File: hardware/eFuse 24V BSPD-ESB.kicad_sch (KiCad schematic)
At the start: 9 parts, among them IC3 NCS20061MUTAG_IMG, IC6 NIS4461MT1TXG

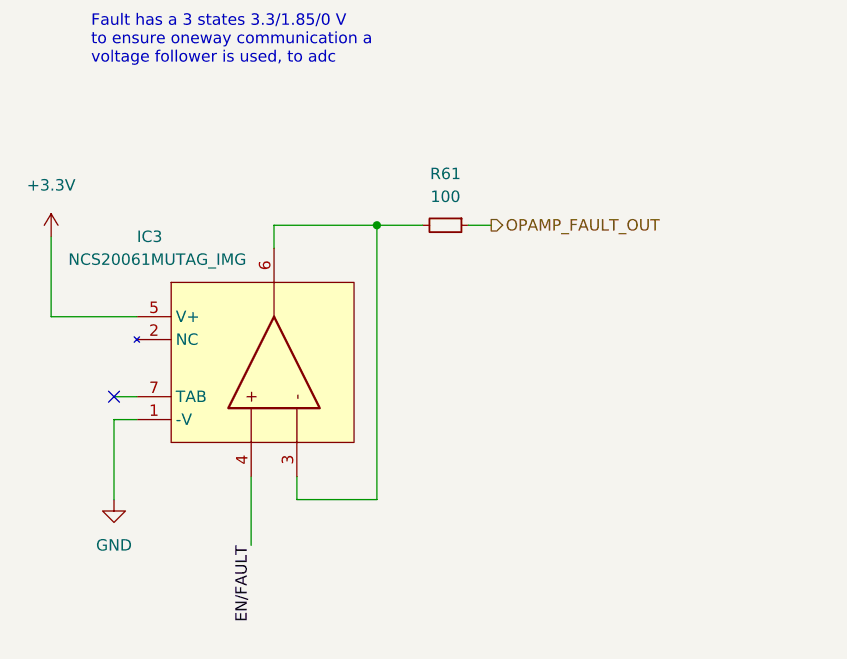
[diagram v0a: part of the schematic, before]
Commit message: debuged the board, changed one opto for mosfet, changed the way water and potentiometers were supplied. Also standrised opamps (yoinked opamps from data Data_Acquisition_Cards)
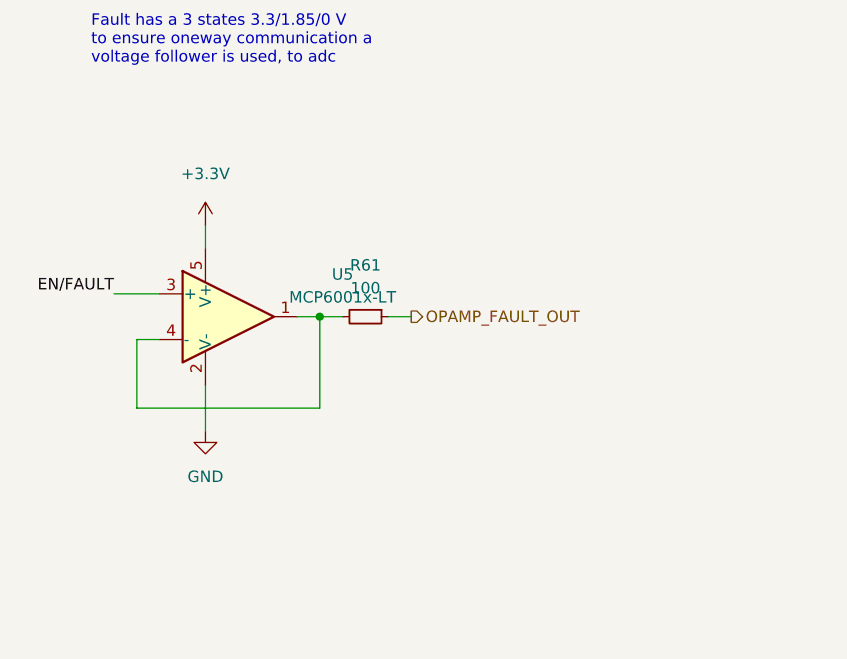
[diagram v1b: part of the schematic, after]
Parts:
- removed IC3: NCS20061MUTAG_IMG, NCS20061MUTAG:SON50P160X160X55-7N, symbol NCS20061MUTAG:NCS20061MUTAG_IMG
- added U5: MCP6001x-LT, Package_TO_SOT_SMD:SOT-353_SC-70-5, symbol Amplifier_Operational:MCP6001x-LT
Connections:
- net +3V3: now also U5.5 (V+)
- net EN/FAULT: now also U5.3 (+)
- net GND: now also U5.2 (V-)
- net at R61.2: now also U5.1, U5.4 (-)
- no-connect marks 1 -> 0
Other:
- moved on the sheet: R61
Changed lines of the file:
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@@
   (junction (at 220.98 99.06) (diameter 0) (color 0 0 0 0)
   )
-  (junction (at 92.71 67.31) (diameter 0) (color 0 0 0 0)
+  (junction (at 86.36 77.47) (diameter 0) (color 0 0 0 0)
   )
   (junction (at 234.315 73.025) (diameter 0) (color 0 0 0 0)
@@
   (junction (at 180.34 83.185) (diameter 0) (color 0 0 0 0)
   )
-  (no_connect (at 63.5 86.36))
-  (wire (pts (xy 92.71 67.31) (xy 97.79 67.31))
+  (wire (pts (xy 83.82 77.47) (xy 86.36 77.47))
     (stroke (width 0) (type default) (color 0 0 0 0))
   )
@@
     (stroke (width 0) (type default) (color 0 0 0 0))
   )
-  (wire (pts (xy 56.515 77.47) (xy 66.04 77.47))
-    (stroke (width 0) (type default) (color 0 0 0 0))
-  )
-  (wire (pts (xy 102.87 67.31) (xy 105.41 67.31))
+  (wire (pts (xy 93.98 77.47) (xy 96.52 77.47))
     (stroke (width 0) (type default) (color 0 0 0 0))
   )
@@
     (stroke (width 0) (type default) (color 0 0 0 0))
   )
+  (wire (pts (xy 86.36 77.47) (xy 86.36 87.63))
+    (stroke (width 0) (type default) (color 0 0 0 0))
+  )
   (wire (pts (xy 228.6 95.25) (xy 234.315 95.25))
     (stroke (width 0) (type default) (color 0 0 0 0))
   )
+  (wire (pts (xy 66.04 87.63) (xy 66.04 80.01))
+    (stroke (width 0) (type default) (color 0 0 0 0))
+  )
   (wire (pts (xy 180.34 62.865) (xy 180.34 83.185))
     (stroke (width 0) (type default) (color 0 0 0 0))
   )
-  (wire (pts (xy 56.515 68.58) (xy 56.515 77.47))
+  (wire (pts (xy 73.66 67.31) (xy 73.66 69.85))
     (stroke (width 0) (type default) (color 0 0 0 0))
   )
@@
     (stroke (width 0) (type default) (color 0 0 0 0))
   )
-  (wire (pts (xy 78.74 95.25) (xy 78.74 102.87))
-    (stroke (width 0) (type default) (color 0 0 0 0))
-  )
-  (wire (pts (xy 81.28 67.31) (xy 81.28 69.85))
+  (wire (pts (xy 68.58 74.93) (xy 63.5 74.93))
     (stroke (width 0) (type default) (color 0 0 0 0))
   )
@@
     (stroke (width 0) (type default) (color 0 0 0 0))
   )
-  (wire (pts (xy 63.5 86.36) (xy 66.04 86.36))
-    (stroke (width 0) (type default) (color 0 0 0 0))
-  )
   (wire (pts (xy 186.69 65.405) (xy 186.69 75.565))
     (stroke (width 0) (type default) (color 0 0 0 0))
@@
     (stroke (width 0) (type default) (color 0 0 0 0))
   )
+  (wire (pts (xy 86.36 87.63) (xy 66.04 87.63))
+    (stroke (width 0) (type default) (color 0 0 0 0))
+  )
   (wire (pts (xy 193.675 70.485) (xy 196.215 70.485))
     (stroke (width 0) (type default) (color 0 0 0 0))
   )
-  (wire (pts (xy 66.04 88.9) (xy 63.5 88.9))
-    (stroke (width 0) (type default) (color 0 0 0 0))
-  )
   (wire (pts (xy 220.98 95.25) (xy 223.52 95.25))
     (stroke (width 0) (type default) (color 0 0 0 0))
@@
     (stroke (width 0) (type default) (color 0 0 0 0))
   )
+  (wire (pts (xy 66.04 80.01) (xy 68.58 80.01))
+    (stroke (width 0) (type default) (color 0 0 0 0))
+  )
   (wire (pts (xy 234.315 62.865) (xy 234.315 65.405))
     (stroke (width 0) (type default) (color 0 0 0 0))
@@
     (stroke (width 0) (type default) (color 0 0 0 0))
   )
-  (wire (pts (xy 83.82 95.25) (xy 83.82 97.79))
-    (stroke (width 0) (type default) (color 0 0 0 0))
-  )
   (wire (pts (xy 213.995 91.44) (xy 222.885 91.44))
     (stroke (width 0) (type default) (color 0 0 0 0))
   )
-  (wire (pts (xy 83.82 97.79) (xy 92.71 97.79))
-    (stroke (width 0) (type default) (color 0 0 0 0))
-  )
-  (wire (pts (xy 92.71 67.31) (xy 81.28 67.31))
-    (stroke (width 0) (type default) (color 0 0 0 0))
-  )
   (wire (pts (xy 228.6 102.87) (xy 234.315 102.87))
     (stroke (width 0) (type default) (color 0 0 0 0))
@@
     (stroke (width 0) (type default) (color 0 0 0 0))
   )
-  (wire (pts (xy 92.71 97.79) (xy 92.71 67.31))
-    (stroke (width 0) (type default) (color 0 0 0 0))
-  )
   (wire (pts (xy 173.99 67.945) (xy 196.215 67.945))
     (stroke (width 0) (type default) (color 0 0 0 0))
@@
     (stroke (width 0) (type default) (color 0 0 0 0))
   )
+  (wire (pts (xy 86.36 77.47) (xy 88.9 77.47))
+    (stroke (width 0) (type default) (color 0 0 0 0))
+  )
   (wire (pts (xy 220.98 99.06) (xy 220.98 102.87))
     (stroke (width 0) (type default) (color 0 0 0 0))
@@
     (stroke (width 0) (type default) (color 0 0 0 0))
   )
-  (wire (pts (xy 63.5 88.9) (xy 63.5 97.79))
+  (wire (pts (xy 73.66 85.09) (xy 73.66 90.17))
     (stroke (width 0) (type default) (color 0 0 0 0))
   )
@@
     (effects (font (size 1.27 1.27)) (justify right bottom))
   )
-  (label "EN{slash}FAULT" (at 78.74 102.87 270)
+  (label "EN{slash}FAULT" (at 63.5 74.93 180)
     (effects (font (size 1.27 1.27)) (justify right bottom))
   )
@@
     (effects (font (size 1.27 1.27)) (justify left))
   )
-  (hierarchical_label "OPAMP_FAULT_OUT" (shape output) (at 105.41 67.31 0)
+  (hierarchical_label "OPAMP_FAULT_OUT" (shape output) (at 96.52 77.47 0)
     (effects (font (size 1.27 1.27)) (justify left))
   )
@@
     (pin "1")
   )
-  (symbol (lib_id "power:GND") (at 63.5 97.79 0) (unit 1)
-    (in_bom yes) (on_board yes) (fields_autoplaced)
-    (property "Reference" "#PWR0151" (id 0) (at 63.5 104.14 0)
-      (effects (font (size 1.27 1.27)) hide)
-    )
-    (property "Value" "GND" (id 1) (at 63.5 102.87 0))
-    (property "Footprint" "" (id 2) (at 63.5 97.79 0)
-      (effects (font (size 1.27 1.27)) hide)
-    )
-    (property "Datasheet" "" (id 3) (at 63.5 97.79 0)
+  (symbol (lib_id "power:GND") (at 73.66 90.17 0) (unit 1)
+    (in_bom yes) (on_board yes) (fields_autoplaced)
+    (property "Reference" "#PWR0151" (id 0) (at 73.66 96.52 0)
+      (effects (font (size 1.27 1.27)) hide)
+    )
+    (property "Value" "GND" (id 1) (at 73.66 95.25 0))
+    (property "Footprint" "" (id 2) (at 73.66 90.17 0)
+      (effects (font (size 1.27 1.27)) hide)
+    )
+    (property "Datasheet" "" (id 3) (at 73.66 90.17 0)
       (effects (font (size 1.27 1.27)) hide)
     )
@@
     (pin "1")
     (pin "2")
-  )
-  (symbol (lib_id "NCS20061MUTAG:NCS20061MUTAG_IMG") (at 80.01 64.77 0) (unit 1)
-    (in_bom yes) (on_board yes)
-    (property "Reference" "IC3" (id 0) (at 66.04 68.58 0)
-      (effects (font (size 1.27 1.27)) (justify left))
-    )
-    (property "Value" "NCS20061MUTAG_IMG" (id 1) (at 58.42 71.12 0)
-      (effects (font (size 1.27 1.27)) (justify left))
-    )
-    (property "Footprint" "NCS20061MUTAG:SON50P160X160X55-7N" (id 2) (at 106.68 69.85 0)
-      (effects (font (size 1.27 1.27)) hide)
-    )
-    (property "Datasheet" "" (id 3) (at 81.28 71.12 0)
-      (effects (font (size 1.27 1.27)) hide)
-    )
-    (pin "1")
-    (pin "2")
-    (pin "3")
-    (pin "4")
-    (pin "5")
-    (pin "6")
-    (pin "7")
   )
   (symbol (lib_id "NIS4461MT1TXG:NIS4461MT1TXG") (at 196.215 62.865 0) (unit 1)
@@
     (pin "2")
   )
-  (symbol (lib_id "power:+3.3V") (at 56.515 68.58 0) (unit 1)
-    (in_bom yes) (on_board yes) (fields_autoplaced)
-    (property "Reference" "#PWR0143" (id 0) (at 56.515 72.39 0)
-      (effects (font (size 1.27 1.27)) hide)
-    )
-    (property "Value" "+3.3V" (id 1) (at 56.515 62.865 0))
-    (property "Footprint" "" (id 2) (at 56.515 68.58 0)
-      (effects (font (size 1.27 1.27)) hide)
-    )
-    (property "Datasheet" "" (id 3) (at 56.515 68.58 0)
-      (effects (font (size 1.27 1.27)) hide)
-    )
-    (pin "1")
-  )
-  (symbol (lib_id "Device:R_Small") (at 100.33 67.31 270) (unit 1)
-    (in_bom yes) (on_board yes) (fields_autoplaced)
-    (property "Reference" "R61" (id 0) (at 100.33 61.595 90))
-    (property "Value" "100" (id 1) (at 100.33 64.135 90))
-    (property "Footprint" "Resistor_SMD:R_0603_1608Metric" (id 2) (at 100.33 67.31 0)
-      (effects (font (size 1.27 1.27)) hide)
-    )
-    (property "Datasheet" "~" (id 3) (at 100.33 67.31 0)
+  (symbol (lib_id "power:+3.3V") (at 73.66 67.31 0) (unit 1)
+    (in_bom yes) (on_board yes) (fields_autoplaced)
+    (property "Reference" "#PWR0143" (id 0) (at 73.66 71.12 0)
+      (effects (font (size 1.27 1.27)) hide)
+    )
+    (property "Value" "+3.3V" (id 1) (at 73.66 61.595 0))
+    (property "Footprint" "" (id 2) (at 73.66 67.31 0)
+      (effects (font (size 1.27 1.27)) hide)
+    )
+    (property "Datasheet" "" (id 3) (at 73.66 67.31 0)
+      (effects (font (size 1.27 1.27)) hide)
+    )
+    (pin "1")
+  )
+  (symbol (lib_id "Device:R_Small") (at 91.44 77.47 270) (unit 1)
+    (in_bom yes) (on_board yes) (fields_autoplaced)
+    (property "Reference" "R61" (id 0) (at 91.44 71.755 90))
+    (property "Value" "100" (id 1) (at 91.44 74.295 90))
+    (property "Footprint" "Resistor_SMD:R_0603_1608Metric" (id 2) (at 91.44 77.47 0)
+      (effects (font (size 1.27 1.27)) hide)
+    )
+    (property "Datasheet" "~" (id 3) (at 91.44 77.47 0)
       (effects (font (size 1.27 1.27)) hide)
     )
@@
     (pin "2")
   )
+  (symbol (lib_id "Amplifier_Operational:MCP6001x-LT") (at 76.2 77.47 0) (unit 1)
+    (in_bom yes) (on_board yes) (fields_autoplaced)
+    (property "Reference" "U5" (id 0) (at 88.9 72.771 0))
+    (property "Value" "MCP6001x-LT" (id 1) (at 88.9 75.311 0))
+    (property "Footprint" "Package_TO_SOT_SMD:SOT-353_SC-70-5" (id 2) (at 73.66 82.55 0)
+      (effects (font (size 1.27 1.27)) (justify left) hide)
+    )
+    (property "Datasheet" "http://ww1.microchip.com/downloads/en/DeviceDoc/21733j.pdf" (id 3) (at 76.2 77.47 0)
+      (effects (font (size 1.27 1.27)) hide)
+    )
+    (pin "2")
+    (pin "5")
+    (pin "1")
+    (pin "3")
+    (pin "4")
+  )
 )

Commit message: currected TSAL, cause it can't be controled via external logic
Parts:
- renumbered C19 to C17, C20 to C18, F4 to F1, IC6 to IC2, ILIM7 to ILIM1, ILIM8 to ILIM2, IMON3 to IMON1, R61 to R43, U5 to U7
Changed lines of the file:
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@@
     (effects (font (size 1.27 1.27)) (justify left))
   )
-  (symbol (lib_id "power:GND") (at 180.34 95.25 0) (unit 1)
+  (symbol (lib_id "power:GND") (at 180.34 95.25 0)
     (in_bom yes) (on_board yes) (fields_autoplaced)
-    (property "Reference" "#PWR0152" (id 0) (at 180.34 101.6 0)
+    (property "Reference" "#PWR0155" (id 0) (at 180.34 101.6 0)
       (effects (font (size 1.27 1.27)) hide)
     )
@@
     (pin "1")
   )
-  (symbol (lib_id "power:GND") (at 73.66 90.17 0) (unit 1)
+  (symbol (lib_id "power:GND") (at 73.66 90.17 0)
     (in_bom yes) (on_board yes) (fields_autoplaced)
-    (property "Reference" "#PWR0151" (id 0) (at 73.66 96.52 0)
+    (property "Reference" "#PWR0123" (id 0) (at 73.66 96.52 0)
       (effects (font (size 1.27 1.27)) hide)
     )
@@
     (pin "1")
   )
-  (symbol (lib_id "Device:C_Small") (at 167.64 78.105 0) (unit 1)
+  (symbol (lib_id "Device:C_Small") (at 167.64 78.105 0)
     (in_bom yes) (on_board yes)
-    (property "Reference" "C19" (id 0) (at 161.925 76.835 0)
+    (property "Reference" "C17" (id 0) (at 161.925 76.835 0)
       (effects (font (size 1.27 1.27)) (justify left))
     )
@@
     (pin "2")
   )
-  (symbol (lib_id "Device:R_Small") (at 226.06 102.87 270) (unit 1)
+  (symbol (lib_id "Device:R_Small") (at 226.06 102.87 270)
     (in_bom yes) (on_board yes)
-    (property "Reference" "ILIM8" (id 0) (at 226.06 105.41 90))
+    (property "Reference" "ILIM2" (id 0) (at 226.06 105.41 90))
     (property "Value" "?" (id 1) (at 226.06 107.95 90))
     (property "Footprint" "Resistor_SMD:R_0603_1608Metric" (id 2) (at 226.06 102.87 0)
@@
     (pin "2")
   )
-  (symbol (lib_id "Device:C_Small") (at 186.69 78.105 0) (unit 1)
+  (symbol (lib_id "Device:C_Small") (at 186.69 78.105 0)
     (in_bom yes) (on_board yes)
-    (property "Reference" "C20" (id 0) (at 181.61 76.835 0)
+    (property "Reference" "C18" (id 0) (at 181.61 76.835 0)
       (effects (font (size 1.27 1.27)) (justify left))
     )
@@
     (pin "2")
   )
-  (symbol (lib_id "NIS4461MT1TXG:NIS4461MT1TXG") (at 196.215 62.865 0) (unit 1)
+  (symbol (lib_id "NIS4461MT1TXG:NIS4461MT1TXG") (at 196.215 62.865 0)
     (in_bom yes) (on_board yes) (fields_autoplaced)
-    (property "Reference" "IC6" (id 0) (at 213.995 54.61 0))
+    (property "Reference" "IC2" (id 0) (at 213.995 54.61 0))
     (property "Value" "NIS4461MT1TXG" (id 1) (at 213.995 57.15 0))
     (property "Footprint" "NIS4461MT1TXG:SON50P300X300X80-11N" (id 2) (at 227.965 60.325 0)
@@
     (pin "9")
   )
-  (symbol (lib_id "Device:R_Small") (at 177.8 78.105 0) (unit 1)
+  (symbol (lib_id "Device:R_Small") (at 177.8 78.105 0)
     (in_bom yes) (on_board yes)
-    (property "Reference" "IMON3" (id 0) (at 170.815 76.835 0)
+    (property "Reference" "IMON1" (id 0) (at 170.815 76.835 0)
       (effects (font (size 1.27 1.27)) (justify left))
     )
@@
     (pin "2")
   )
-  (symbol (lib_id "power:+3.3V") (at 73.66 67.31 0) (unit 1)
+  (symbol (lib_id "power:+3.3V") (at 73.66 67.31 0)
     (in_bom yes) (on_board yes) (fields_autoplaced)
-    (property "Reference" "#PWR0143" (id 0) (at 73.66 71.12 0)
+    (property "Reference" "#PWR0135" (id 0) (at 73.66 71.12 0)
       (effects (font (size 1.27 1.27)) hide)
     )
@@
     (pin "1")
   )
-  (symbol (lib_id "Device:R_Small") (at 91.44 77.47 270) (unit 1)
+  (symbol (lib_id "Device:R_Small") (at 91.44 77.47 270)
     (in_bom yes) (on_board yes) (fields_autoplaced)
-    (property "Reference" "R61" (id 0) (at 91.44 71.755 90))
+    (property "Reference" "R43" (id 0) (at 91.44 71.755 90))
     (property "Value" "100" (id 1) (at 91.44 74.295 90))
     (property "Footprint" "Resistor_SMD:R_0603_1608Metric" (id 2) (at 91.44 77.47 0)
@@
     (pin "2")
   )
-  (symbol (lib_id "Device:R_Small") (at 226.06 95.25 270) (unit 1)
+  (symbol (lib_id "Device:R_Small") (at 226.06 95.25 270)
     (in_bom yes) (on_board yes)
-    (property "Reference" "ILIM7" (id 0) (at 226.06 97.79 90))
+    (property "Reference" "ILIM1" (id 0) (at 226.06 97.79 90))
     (property "Value" "?" (id 1) (at 226.06 100.33 90))
     (property "Footprint" "Resistor_SMD:R_0603_1608Metric" (id 2) (at 226.06 95.25 0)
@@
     (pin "2")
   )
-  (symbol (lib_id "Device:Polyfuse") (at 226.695 91.44 270) (unit 1)
+  (symbol (lib_id "Device:Polyfuse") (at 226.695 91.44 270)
     (in_bom yes) (on_board yes)
-    (property "Reference" "F4" (id 0) (at 226.695 88.9 90))
+    (property "Reference" "F1" (id 0) (at 226.695 88.9 90))
     (property "Value" "Polyfuse" (id 1) (at 226.695 88.0364 90)
       (effects (font (size 1.27 1.27)) hide)
@@
     (pin "2")
   )
-  (symbol (lib_id "Amplifier_Operational:MCP6001x-LT") (at 76.2 77.47 0) (unit 1)
+  (symbol (lib_id "Amplifier_Operational:MCP6001x-LT") (at 76.2 77.47 0)
     (in_bom yes) (on_board yes) (fields_autoplaced)
-    (property "Reference" "U5" (id 0) (at 88.9 72.771 0))
+    (property "Reference" "U7" (id 0) (at 88.9 72.771 0))
     (property "Value" "MCP6001x-LT" (id 1) (at 88.9 75.311 0))
     (property "Footprint" "Package_TO_SOT_SMD:SOT-353_SC-70-5" (id 2) (at 73.66 82.55 0)

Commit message: nameing scheme update
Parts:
- renumbered C17 to C19, C18 to C20, F1 to F4, IC2 to IC6, ILIM1 to ILIM7, ILIM2 to ILIM8, IMON1 to IMON3, R43 to R61, U7 to U5
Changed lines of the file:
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@@
   (symbol (lib_id "power:GND") (at 180.34 95.25 0)
     (in_bom yes) (on_board yes) (fields_autoplaced)
-    (property "Reference" "#PWR0155" (id 0) (at 180.34 101.6 0)
+    (property "Reference" "#PWR0152" (id 0) (at 180.34 101.6 0)
       (effects (font (size 1.27 1.27)) hide)
     )
@@
   (symbol (lib_id "power:GND") (at 73.66 90.17 0)
     (in_bom yes) (on_board yes) (fields_autoplaced)
-    (property "Reference" "#PWR0123" (id 0) (at 73.66 96.52 0)
+    (property "Reference" "#PWR0151" (id 0) (at 73.66 96.52 0)
       (effects (font (size 1.27 1.27)) hide)
     )
@@
   (symbol (lib_id "Device:C_Small") (at 167.64 78.105 0)
     (in_bom yes) (on_board yes)
-    (property "Reference" "C17" (id 0) (at 161.925 76.835 0)
+    (property "Reference" "C19" (id 0) (at 161.925 76.835 0)
       (effects (font (size 1.27 1.27)) (justify left))
     )
@@
   (symbol (lib_id "Device:R_Small") (at 226.06 102.87 270)
     (in_bom yes) (on_board yes)
-    (property "Reference" "ILIM2" (id 0) (at 226.06 105.41 90))
+    (property "Reference" "ILIM8" (id 0) (at 226.06 105.41 90))
     (property "Value" "?" (id 1) (at 226.06 107.95 90))
     (property "Footprint" "Resistor_SMD:R_0603_1608Metric" (id 2) (at 226.06 102.87 0)
@@
   (symbol (lib_id "Device:C_Small") (at 186.69 78.105 0)
     (in_bom yes) (on_board yes)
-    (property "Reference" "C18" (id 0) (at 181.61 76.835 0)
+    (property "Reference" "C20" (id 0) (at 181.61 76.835 0)
       (effects (font (size 1.27 1.27)) (justify left))
     )
@@
   (symbol (lib_id "NIS4461MT1TXG:NIS4461MT1TXG") (at 196.215 62.865 0)
     (in_bom yes) (on_board yes) (fields_autoplaced)
-    (property "Reference" "IC2" (id 0) (at 213.995 54.61 0))
+    (property "Reference" "IC6" (id 0) (at 213.995 54.61 0))
     (property "Value" "NIS4461MT1TXG" (id 1) (at 213.995 57.15 0))
     (property "Footprint" "NIS4461MT1TXG:SON50P300X300X80-11N" (id 2) (at 227.965 60.325 0)
@@
   (symbol (lib_id "Device:R_Small") (at 177.8 78.105 0)
     (in_bom yes) (on_board yes)
-    (property "Reference" "IMON1" (id 0) (at 170.815 76.835 0)
+    (property "Reference" "IMON3" (id 0) (at 170.815 76.835 0)
       (effects (font (size 1.27 1.27)) (justify left))
     )
@@
   (symbol (lib_id "power:+3.3V") (at 73.66 67.31 0)
     (in_bom yes) (on_board yes) (fields_autoplaced)
-    (property "Reference" "#PWR0135" (id 0) (at 73.66 71.12 0)
+    (property "Reference" "#PWR0143" (id 0) (at 73.66 71.12 0)
       (effects (font (size 1.27 1.27)) hide)
     )
@@
   (symbol (lib_id "Device:R_Small") (at 91.44 77.47 270)
     (in_bom yes) (on_board yes) (fields_autoplaced)
-    (property "Reference" "R43" (id 0) (at 91.44 71.755 90))
+    (property "Reference" "R61" (id 0) (at 91.44 71.755 90))
     (property "Value" "100" (id 1) (at 91.44 74.295 90))
     (property "Footprint" "Resistor_SMD:R_0603_1608Metric" (id 2) (at 91.44 77.47 0)
@@
   (symbol (lib_id "Device:R_Small") (at 226.06 95.25 270)
     (in_bom yes) (on_board yes)
-    (property "Reference" "ILIM1" (id 0) (at 226.06 97.79 90))
+    (property "Reference" "ILIM7" (id 0) (at 226.06 97.79 90))
     (property "Value" "?" (id 1) (at 226.06 100.33 90))
     (property "Footprint" "Resistor_SMD:R_0603_1608Metric" (id 2) (at 226.06 95.25 0)
@@
   (symbol (lib_id "Device:Polyfuse") (at 226.695 91.44 270)
     (in_bom yes) (on_board yes)
-    (property "Reference" "F1" (id 0) (at 226.695 88.9 90))
+    (property "Reference" "F4" (id 0) (at 226.695 88.9 90))
     (property "Value" "Polyfuse" (id 1) (at 226.695 88.0364 90)
       (effects (font (size 1.27 1.27)) hide)
@@
   (symbol (lib_id "Amplifier_Operational:MCP6001x-LT") (at 76.2 77.47 0)
     (in_bom yes) (on_board yes) (fields_autoplaced)
-    (property "Reference" "U7" (id 0) (at 88.9 72.771 0))
+    (property "Reference" "U5" (id 0) (at 88.9 72.771 0))
     (property "Value" "MCP6001x-LT" (id 1) (at 88.9 75.311 0))
     (property "Footprint" "Package_TO_SOT_SMD:SOT-353_SC-70-5" (id 2) (at 73.66 82.55 0)
